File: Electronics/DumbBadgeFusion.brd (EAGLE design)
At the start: 163.5 x 113 mm, 139 parts, among them IC1 74245MTC, IC2 74245MTC, IC3 74245MTC, SW1 SPST_TACT-KMR2, T1 MMUN2133LT1G, U1 TDP3E001DRLR-SOT-23-5SOT-23-5, U2 TPS61090RSAR, U3 MCP73871, U4 FAN5333BSX, U6 MAX3232, X4 32.768

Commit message: more power supply
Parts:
- R12: value 6 -> 6Ω
- moved R1 19.5 mm to (40.6, 57.5)
- moved C8 14.8 mm to (36.8, 61.0), turned to 0 degrees
- moved R12 12.2 mm to (40.6, 61.2), turned to 270 degrees
- moved C9 12.1 mm to (42.8, 61.2), turned to 90 degrees
- moved VREG 11.9 mm to (12.5, 106.0), turned to 270 degrees
- moved C10 9.88 mm to (38.6, 68.5), turned to 180 degrees
- moved U4 9.83 mm to (36.8, 57.5), turned to 180 degrees
- moved D1 8.69 mm to (39.1, 65.5), turned to 180 degrees
- moved D2 5.83 mm to (31.4, 64.0), turned to 0 degrees
- moved C11 4.88 mm to (36.8, 62.7), turned to 180 degrees
- moved C5 3.87 mm to (19.3, 106.9), turned to 90 degrees
- moved L2 3.42 mm to (31.2, 59.3), turned to 90 degrees
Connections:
- removed net N$21: C8.1, L2.P$1, R1.2, U4.5
- net 5.0V: now also C8.1, L2.P$1, R1.2, U4.5
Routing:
- net 5.0V: track 6.08 -> 77.6 mm, vias 0 -> 2
- net LEDK: track 0.00 -> 28.0 mm
- net +24V: track 0.00 -> 16.9 mm
- net N$20: track 0.00 -> 10.9 mm
- net GND: track 33.5 -> 43.9 mm
- net PWM: track 0.00 -> 4.07 mm

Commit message: more power supply
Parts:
- moved U$4 71.5 mm to (139.7, 74.9)
- moved C4 13.2 mm to (15.3, 81.9), turned to 90 degrees
- moved C2 12.2 mm to (17.3, 81.9), turned to 90 degrees
- moved R7 7.39 mm to (17.8, 86.9), turned to 90 degrees
- moved U$32 4.02 mm to (233.7, 62.2)
- moved R8 3.07 mm to (13.6, 81.8), turned to 270 degrees
- moved B2 0.13 mm to (6.27, 59.6)
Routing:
- net 5.0V: track 77.6 -> 108.1 mm
- net +24V: track 16.9 -> 45.1 mm, vias 0 -> 2
- net LEDK: track 28.0 -> 54.5 mm, vias 0 -> 2
- net VBAT: track 2.53 -> 26.0 mm, vias 0 -> 2
- net VBUS: track 359.3 -> 370.8 mm, vias 2 -> 4
- net GND: track 43.9 -> 36.1 mm
- net N$4: track 7.36 -> 0.00 mm
- net VLIPO: track 37.0 -> 38.8 mm

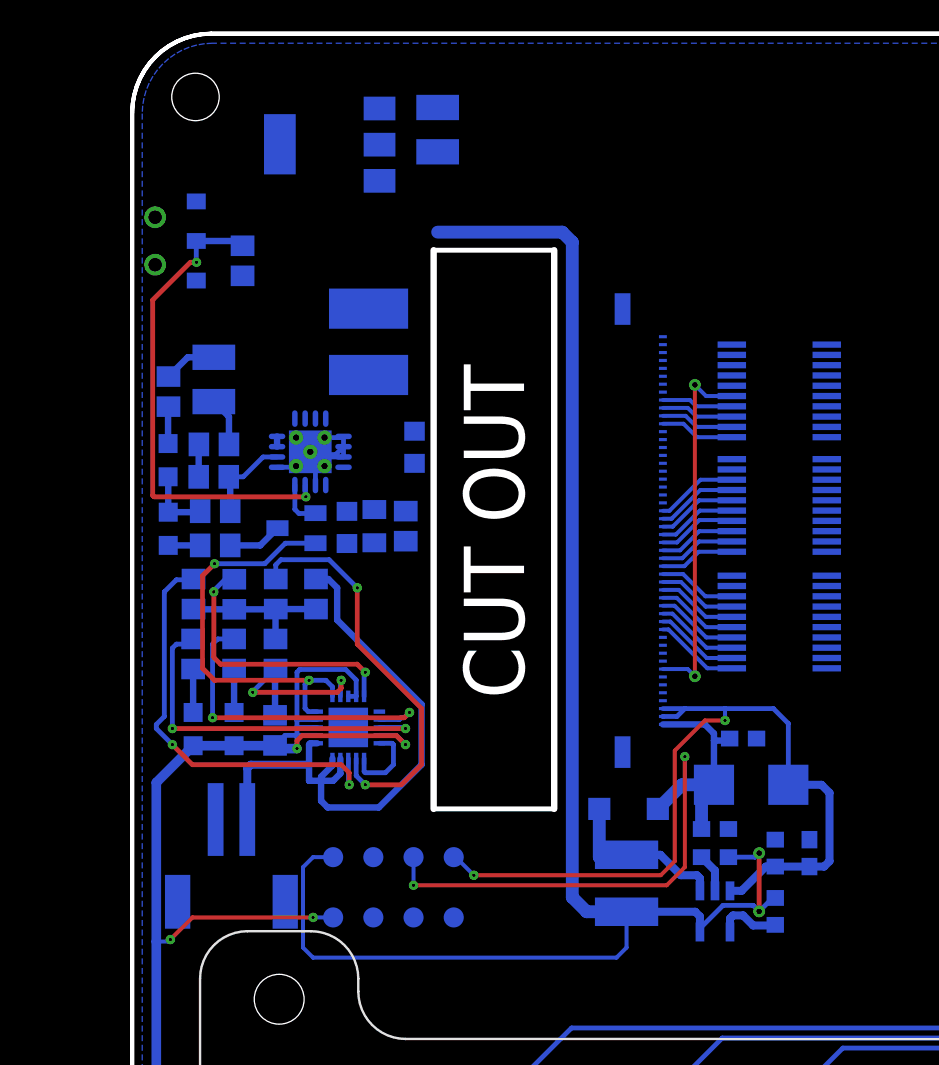
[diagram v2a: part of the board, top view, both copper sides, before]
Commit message: redid and prettified power supply
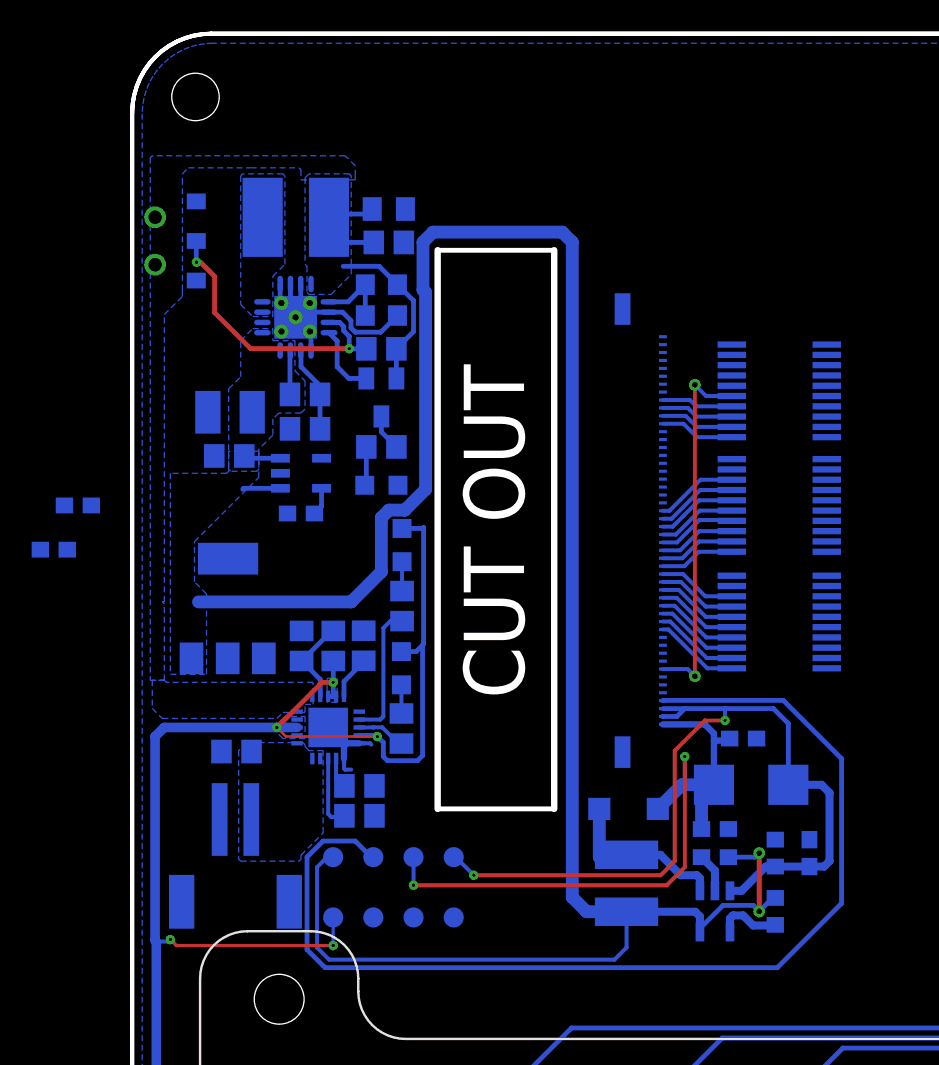
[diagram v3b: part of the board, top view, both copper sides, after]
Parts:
- removed CHRG/LBO: ORANGE, microbuilder:CHIPLED_0805_NOOUTLINE
- removed LED2: BLUE, microbuilder:CHIPLED_0805_NOOUTLINE
- removed NCP21XW153J03RA: 15K, microbuilder:0805-NO
- added BATT_LOW: ORANGE, microbuilder:CHIPLED_0805_NOOUTLINE
- added C13, C14: 1.0uF, SparkFun-Capacitors:0603
- added U5: ADP160AUJZ-1.8-R7, SparkFun-IC-Power:SOT23-5
- C5: value 100uF -> 1.0uF; device rcl:C1210 -> SparkFun-Capacitors:0603
- R5: value 1K -> NCP21XW153J03RA
- moved C5 32.9 mm to (-3.43, 83.2), turned to 180 degrees
- moved VREG 30.0 mm to (6.06, 76.7), turned to 0 degrees
- moved R5 20.3 mm to (14.6, 74.3)
- moved C4 20.1 mm to (16.2, 101.9), turned to 180 degrees
- moved C2 18.0 mm to (16.2, 99.8), turned to 180 degrees
- moved R16 17.5 mm to (14.4, 63.6), turned to 0 degrees
- moved DONE 15.7 mm to (17.1, 80.7), turned to 180 degrees
- moved R8 15.5 mm to (15.7, 97.1), turned to 180 degrees
- moved R11 14.0 mm to (17.0, 69.1), turned to 90 degrees
- moved LED1 13.7 mm to (15.7, 84.5), turned to 90 degrees
- moved R17 13.2 mm to (14.4, 65.5), turned to 0 degrees
- moved R20 12.2 mm to (15.7, 86.9)
- moved C7 11.1 mm to (6.59, 67.6), turned to 0 degrees
- moved R14 11.0 mm to (17.1, 76.8), turned to 90 degrees
- moved R13 10.4 mm to (15.7, 93.1), turned to 0 degrees
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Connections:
- removed net N$9: LED2.A, R5.2
- new net 1.8V: C14.1, U5.5
- net 5.0V: now also C13.1, U5.1, U5.3; no longer R5.1
- net GND: now also C13.2, C14.2, R5.1, U5.2; no longer LED2.C, NCP21XW153J03RA.1
- net N$14: now also R5.2; no longer NCP21XW153J03RA.2
- net N$18: now also BATT_LOW.C; no longer CHRG/LBO.C
- net VBUS: now also BATT_LOW.A; no longer CHRG/LBO.A
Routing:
- net 3V3: track 0.00 -> 68.8 mm
- net VLIPO: track 38.8 -> 0.00 mm
- net 5.0V: track 108.1 -> 144.1 mm
- net N$19: track 25.8 -> 1.95 mm, vias 2 -> 0
- net N$16: track 26.8 -> 4.71 mm, vias 2 -> 0
- net N$13: track 23.0 -> 3.09 mm, vias 2 -> 0
- net VBUS: track 370.8 -> 386.4 mm, vias 4 -> 5
- net N$14: track 17.4 -> 2.76 mm, vias 2 -> 0
- net GND: track 36.1 -> 22.4 mm
- net N$11: track 20.8 -> 8.55 mm, vias 2 -> 0
- net ENABLE: track 31.0 -> 19.0 mm
- net VBAT: track 26.0 -> 17.5 mm, vias 2 -> 0
- net N$10: track 12.2 -> 5.52 mm, vias 2 -> 0
- net N$4: track 0.00 -> 4.71 mm
- net N$9: track 2.34 -> 0.00 mm
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- added copper zone on layer 16, net 5.0V
- added copper zone on layer 16, net N$2
- added copper zone on layer 16, net VBAT
- added copper zone on layer 16, net VBUS
- added copper zone on layer 16, net VLIPO
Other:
- outline, holes or cut-outs redrawn
- board text added: "Low Batt"

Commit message: lots of updating
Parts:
- removed B2: JST 2-PH, microbuilder:JSTPH2
- removed C13: 1.0uF, SparkFun-Capacitors:0603
- removed U5: ADP160AUJZ-1.8-R7, SparkFun-IC-Power:SOT23-5
- added B1: JST 2-PH, microbuilder:JSTPH2
- added R15: 1K, microbuilder:0805-NO
- added R18: 1.2K, microbuilder:0805-NO
- added TP10, TP9: TPB1,27, testpad:B1,27
- moved U$32 121.4 mm to (115.6, 90.2)
- moved C22 118.0 mm to (63.6, 104.1), turned to 270 degrees
- moved C23 114.4 mm to (63.6, 100.4), turned to 270 degrees
- moved U6 109.3 mm to (69.2, 101.0), turned to 270 degrees
- moved C24 108.0 mm to (74.1, 104.0), turned to 270 degrees
- moved SW1 104.7 mm to (86.8, 109.6), turned to 180 degrees
- moved C27 93.9 mm to (92.9, 104.1), turned to 180 degrees
- moved C26 90.7 mm to (92.9, 101.6), turned to 180 degrees
- moved X4 90.4 mm to (86.3, 97.5), turned to 270 degrees
- moved C28 84.7 mm to (98.9, 99.8), turned to 180 degrees
- moved TP6 16.7 mm to (29.6, 52.3)
- moved TP5 16.7 mm to (27.1, 52.3)
- moved TP7 16.7 mm to (32.1, 52.3)
- moved TP8 16.7 mm to (34.7, 52.3)
- moved C5 13.5 mm to (7.24, 74.9), turned to 0 degrees
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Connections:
- net 1.8V: now also R15.1, R18.2, TP9.TP; no longer U5.5
- net 3V3: now also R15.2
- net 5.0V: no longer C13.1, U5.1, U5.3
- net GND: now also B1.1, R18.1, TP10.TP; no longer B2.1, C13.2, U5.2
- net VLIPO: now also B1.2; no longer B2.2
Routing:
- net 1.8V: track 1.78 -> 128.3 mm, vias 0 -> 3
- net 3V3: track 68.8 -> 138.9 mm, vias 0 -> 3
- net GND: track 22.4 -> 90.0 mm, vias 0 -> 20
- net VBAT: track 17.5 -> 51.1 mm, vias 0 -> 2
- net VLIPO: track 0.00 -> 23.4 mm
- net 5.0V: track 144.1 -> 123.2 mm
- net +24V: track 45.1 -> 34.9 mm
- net VBUS: track 386.4 -> 391.1 mm, vias 5 -> 3
- net N$19: track 1.95 -> 4.38 mm
- net N$16: track 4.71 -> 2.45 mm
- added copper zone on layer 1, net GND
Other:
- outline, holes or cut-outs redrawn
- board text added: "1V8"
- board text added: "GND"
- board text added: "V+"

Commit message: modified models
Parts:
- added TP11, TP12, TP13, TP14, TP15, TP16: TPB1,27, testpad:B1,27
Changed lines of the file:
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@@
 <setting verticaltext="up"/>
 </settings>
-<grid distance="50" unitdist="mil" unit="mil" style="lines" multiple="1" display="no" altdistance="5" altunitdist="mil" altunit="mil"/>
+<grid distance="100" unitdist="mil" unit="mil" style="lines" multiple="1" display="no" altdistance="5" altunitdist="mil" altunit="mil"/>
 <layers>
 <layer number="1" name="Top" color="4" fill="1" visible="yes" active="yes"/>
@@
 <attribute name="VALUE" x="40.513" y="51.562" size="0.0254" layer="28" rot="MR0"/>
 </element>
+<element name="TP11" library="testpad" library_urn="urn:adsk.eagle:library:385" package="B1,27" package3d_urn="urn:adsk.eagle:package:27944/2" value="TPB1,27" x="93.218" y="52.324" smashed="yes" rot="MR0">
+<attribute name="NAME" x="94.107" y="53.34" size="0.6096" layer="26" font="vector" ratio="20" rot="MR0"/>
+<attribute name="POPULARITY" value="19" x="93.218" y="52.324" size="1.27" layer="28" font="vector" ratio="14" rot="MR0" display="off"/>
+<attribute name="TP_SIGNAL_NAME" value="" x="93.853" y="50.419" size="1" layer="38" rot="MR0"/>
+<attribute name="VALUE" x="93.853" y="51.562" size="0.0254" layer="28" rot="MR0"/>
+</element>
+<element name="TP12" library="testpad" library_urn="urn:adsk.eagle:library:385" package="B1,27" package3d_urn="urn:adsk.eagle:package:27944/2" value="TPB1,27" x="95.758" y="52.324" smashed="yes" rot="MR0">
+<attribute name="NAME" x="96.647" y="53.34" size="0.6096" layer="26" font="vector" ratio="20" rot="MR0"/>
+<attribute name="POPULARITY" value="19" x="95.758" y="52.324" size="1.27" layer="28" font="vector" ratio="14" rot="MR0" display="off"/>
+<attribute name="TP_SIGNAL_NAME" value="" x="96.393" y="50.419" size="1" layer="38" rot="MR0"/>
+<attribute name="VALUE" x="96.393" y="51.562" size="0.0254" layer="28" rot="MR0"/>
+</element>
+<element name="TP13" library="testpad" library_urn="urn:adsk.eagle:library:385" package="B1,27" package3d_urn="urn:adsk.eagle:package:27944/2" value="TPB1,27" x="98.298" y="52.324" smashed="yes" rot="MR0">
+<attribute name="NAME" x="99.187" y="53.34" size="0.6096" layer="26" font="vector" ratio="20" rot="MR0"/>
+<attribute name="POPULARITY" value="19" x="98.298" y="52.324" size="1.27" layer="28" font="vector" ratio="14" rot="MR0" display="off"/>
+<attribute name="TP_SIGNAL_NAME" value="" x="98.933" y="50.419" size="1" layer="38" rot="MR0"/>
+<attribute name="VALUE" x="98.933" y="51.562" size="0.0254" layer="28" rot="MR0"/>
+</element>
+<element name="TP14" library="testpad" library_urn="urn:adsk.eagle:library:385" package="B1,27" package3d_urn="urn:adsk.eagle:package:27944/2" value="TPB1,27" x="100.838" y="52.324" smashed="yes" rot="MR0">
+<attribute name="NAME" x="101.727" y="53.34" size="0.6096" layer="26" font="vector" ratio="20" rot="MR0"/>
+<attribute name="POPULARITY" value="19" x="100.838" y="52.324" size="1.27" layer="28" font="vector" ratio="14" rot="MR0" display="off"/>
+<attribute name="TP_SIGNAL_NAME" value="" x="101.473" y="50.419" size="1" layer="38" rot="MR0"/>
+<attribute name="VALUE" x="101.473" y="51.562" size="0.0254" layer="28" rot="MR0"/>
+</element>
+<element name="TP15" library="testpad" library_urn="urn:adsk.eagle:library:385" package="B1,27" package3d_urn="urn:adsk.eagle:package:27944/2" value="TPB1,27" x="103.378" y="52.324" smashed="yes" rot="MR0">
+<attribute name="NAME" x="104.267" y="53.34" size="0.6096" layer="26" font="vector" ratio="20" rot="MR0"/>
+<attribute name="POPULARITY" value="19" x="103.378" y="52.324" size="1.27" layer="28" font="vector" ratio="14" rot="MR0" display="off"/>
+<attribute name="TP_SIGNAL_NAME" value="" x="104.013" y="50.419" size="1" layer="38" rot="MR0"/>
+<attribute name="VALUE" x="104.013" y="51.562" size="0.0254" layer="28" rot="MR0"/>
+</element>
+<element name="TP16" library="testpad" library_urn="urn:adsk.eagle:library:385" package="B1,27" package3d_urn="urn:adsk.eagle:package:27944/2" value="TPB1,27" x="105.918" y="52.324" smashed="yes" rot="MR0">
+<attribute name="NAME" x="106.807" y="53.34" size="0.6096" layer="26" font="vector" ratio="20" rot="MR0"/>
+<attribute name="POPULARITY" value="19" x="105.918" y="52.324" size="1.27" layer="28" font="vector" ratio="14" rot="MR0" display="off"/>
+<attribute name="TP_SIGNAL_NAME" value="" x="106.553" y="50.419" size="1" layer="38" rot="MR0"/>
+<attribute name="VALUE" x="106.553" y="51.562" size="0.0254" layer="28" rot="MR0"/>
+</element>
 </elements>

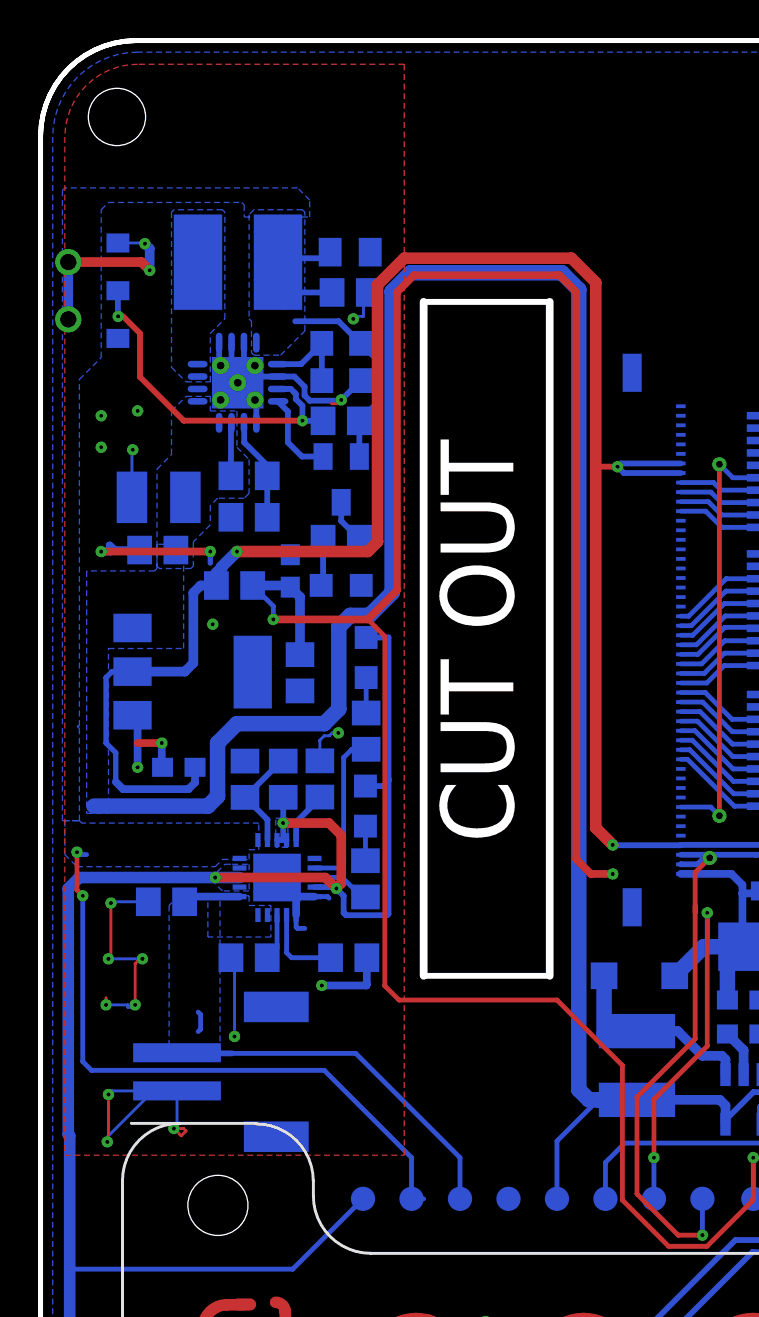
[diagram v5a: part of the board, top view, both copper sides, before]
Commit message: fixed hole for fpc
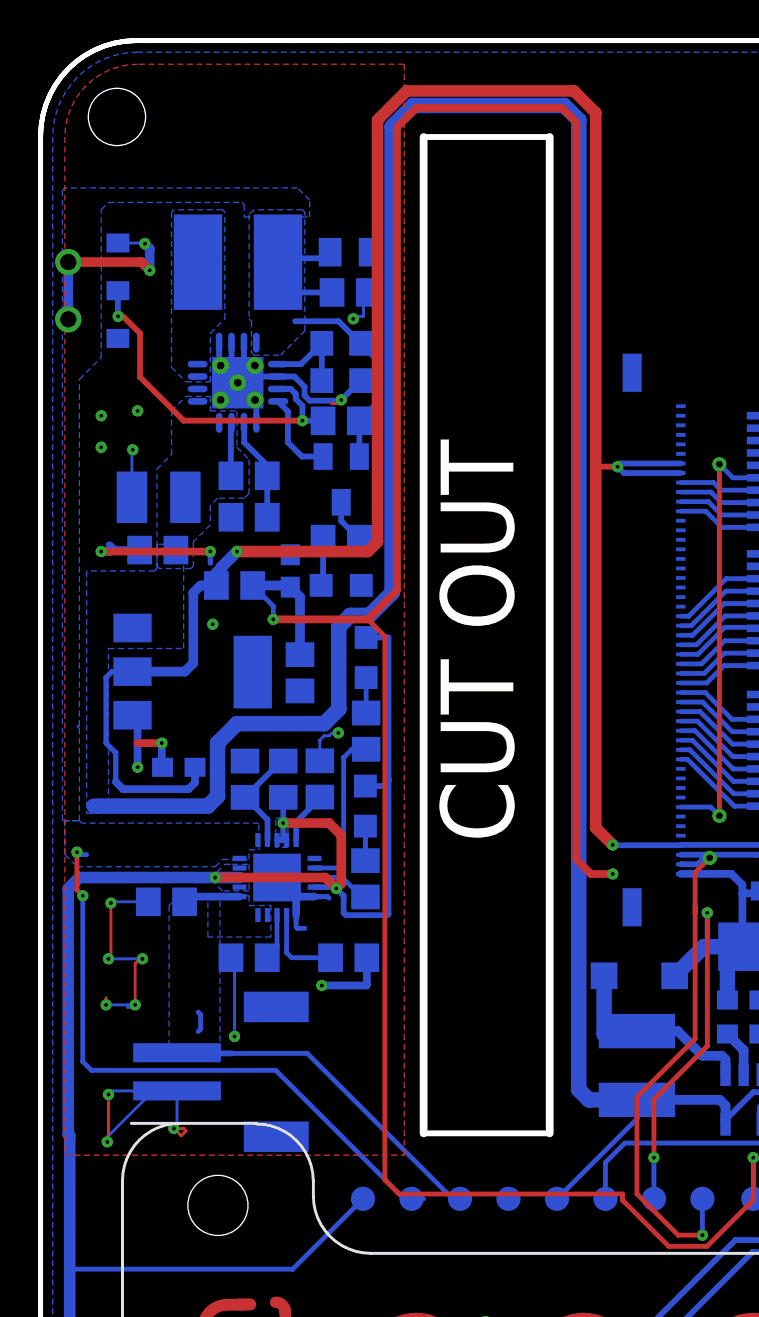
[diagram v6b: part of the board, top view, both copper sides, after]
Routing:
- net 1.8V: track 128.3 -> 147.9 mm
- net 3V3: track 138.9 -> 156.4 mm
- net 5.0V: track 123.2 -> 140.0 mm
- net VLIPO: track 23.4 -> 22.2 mm
- net VBAT: track 51.1 -> 49.8 mm
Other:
- outline, holes or cut-outs redrawn

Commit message: got the display working
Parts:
- moved U$32 38.1 mm to (153.7, 88.9)
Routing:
- net VLIPO: track 22.2 -> 29.6 mm, vias 0 -> 2
- net GND: track 90.0 -> 92.0 mm, vias 20 -> 24
- net 3V3: track 156.4 -> 157.3 mm
- net 5.0V: track 140.0 -> 140.9 mm
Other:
- outline, holes or cut-outs redrawn
